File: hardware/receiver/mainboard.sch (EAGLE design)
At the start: 19 parts, among them J2 POWER_JACKPTH, J3 AVR_SPI_PRG_6PTH, Q1 MOSFET-NCHANNELAO3404A, U1 ATMEGA328P_TQFP, U2 RFM69HCW, U4 RELAY-9007

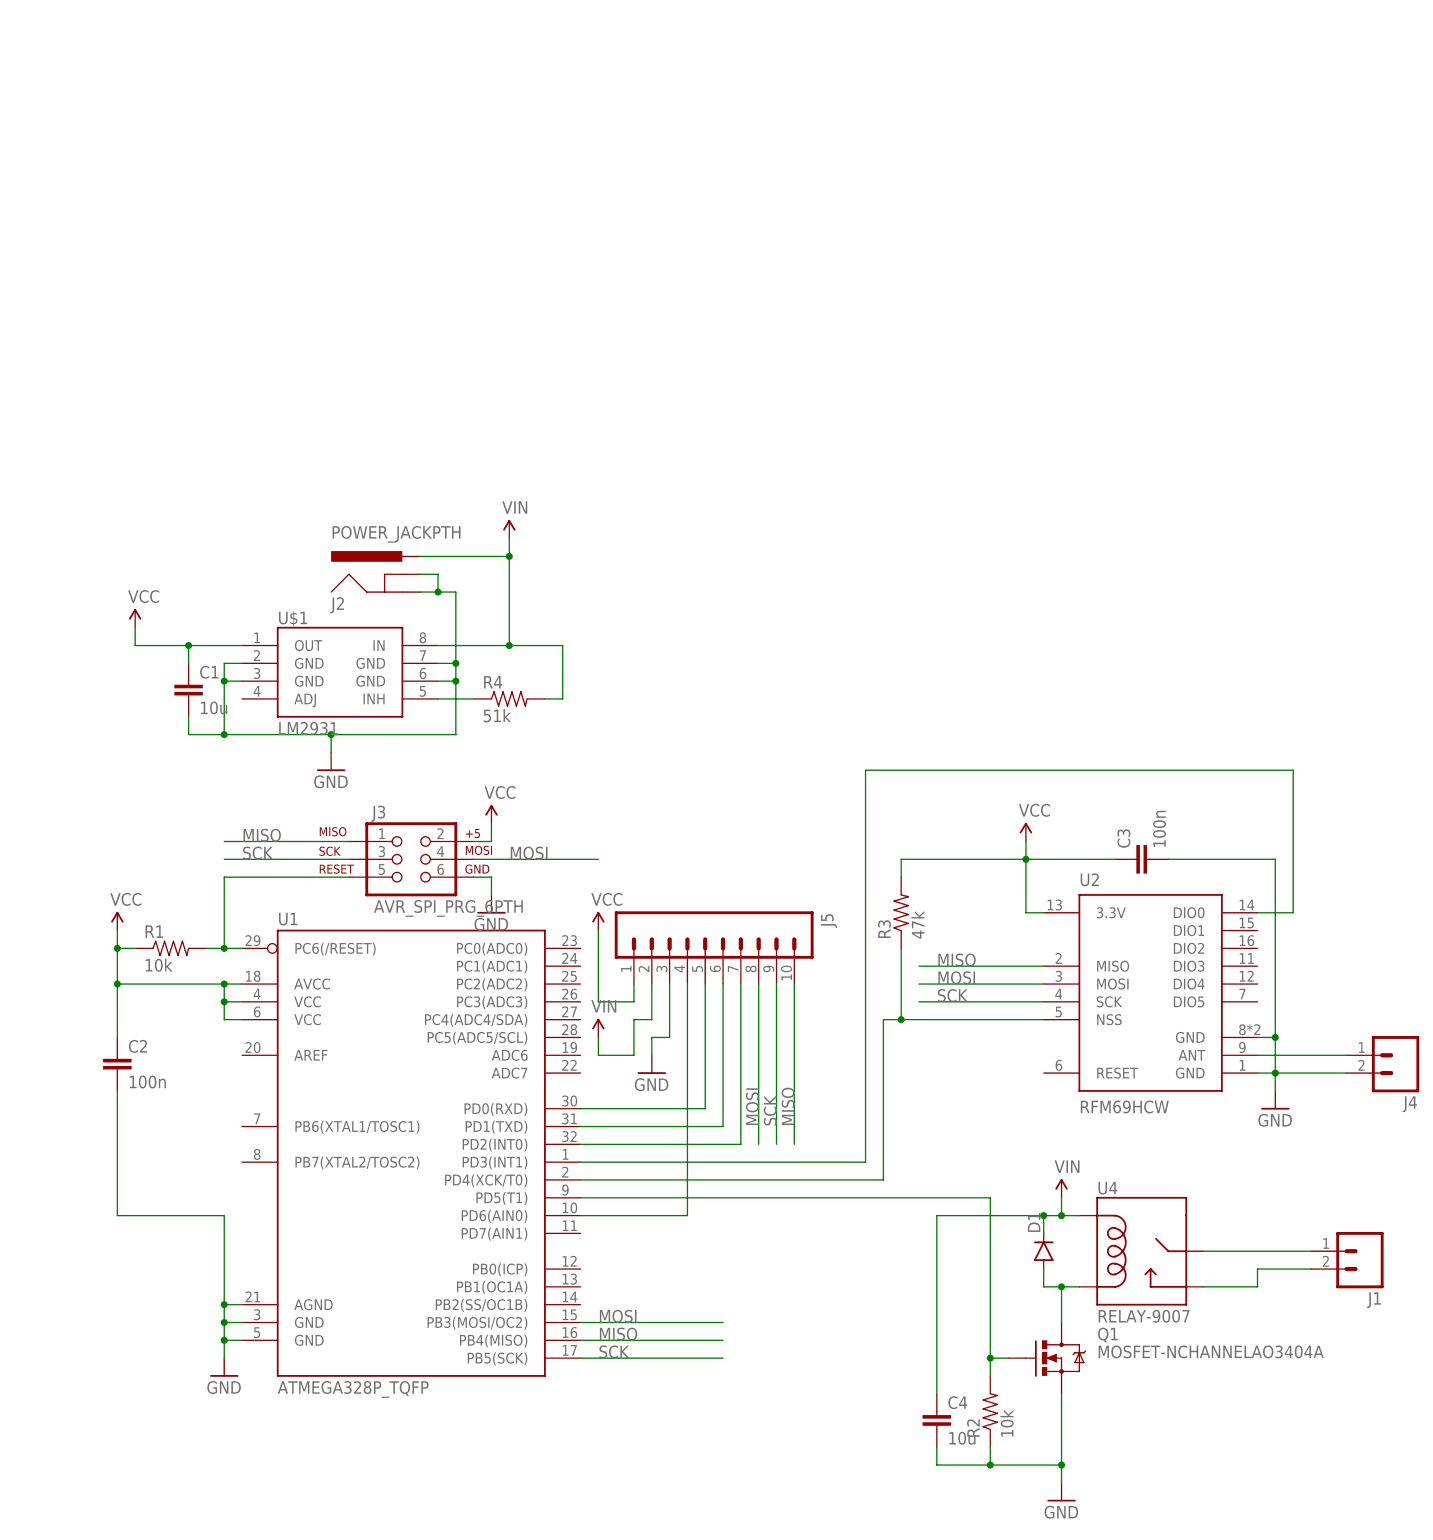
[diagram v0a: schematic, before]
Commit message: Added frames
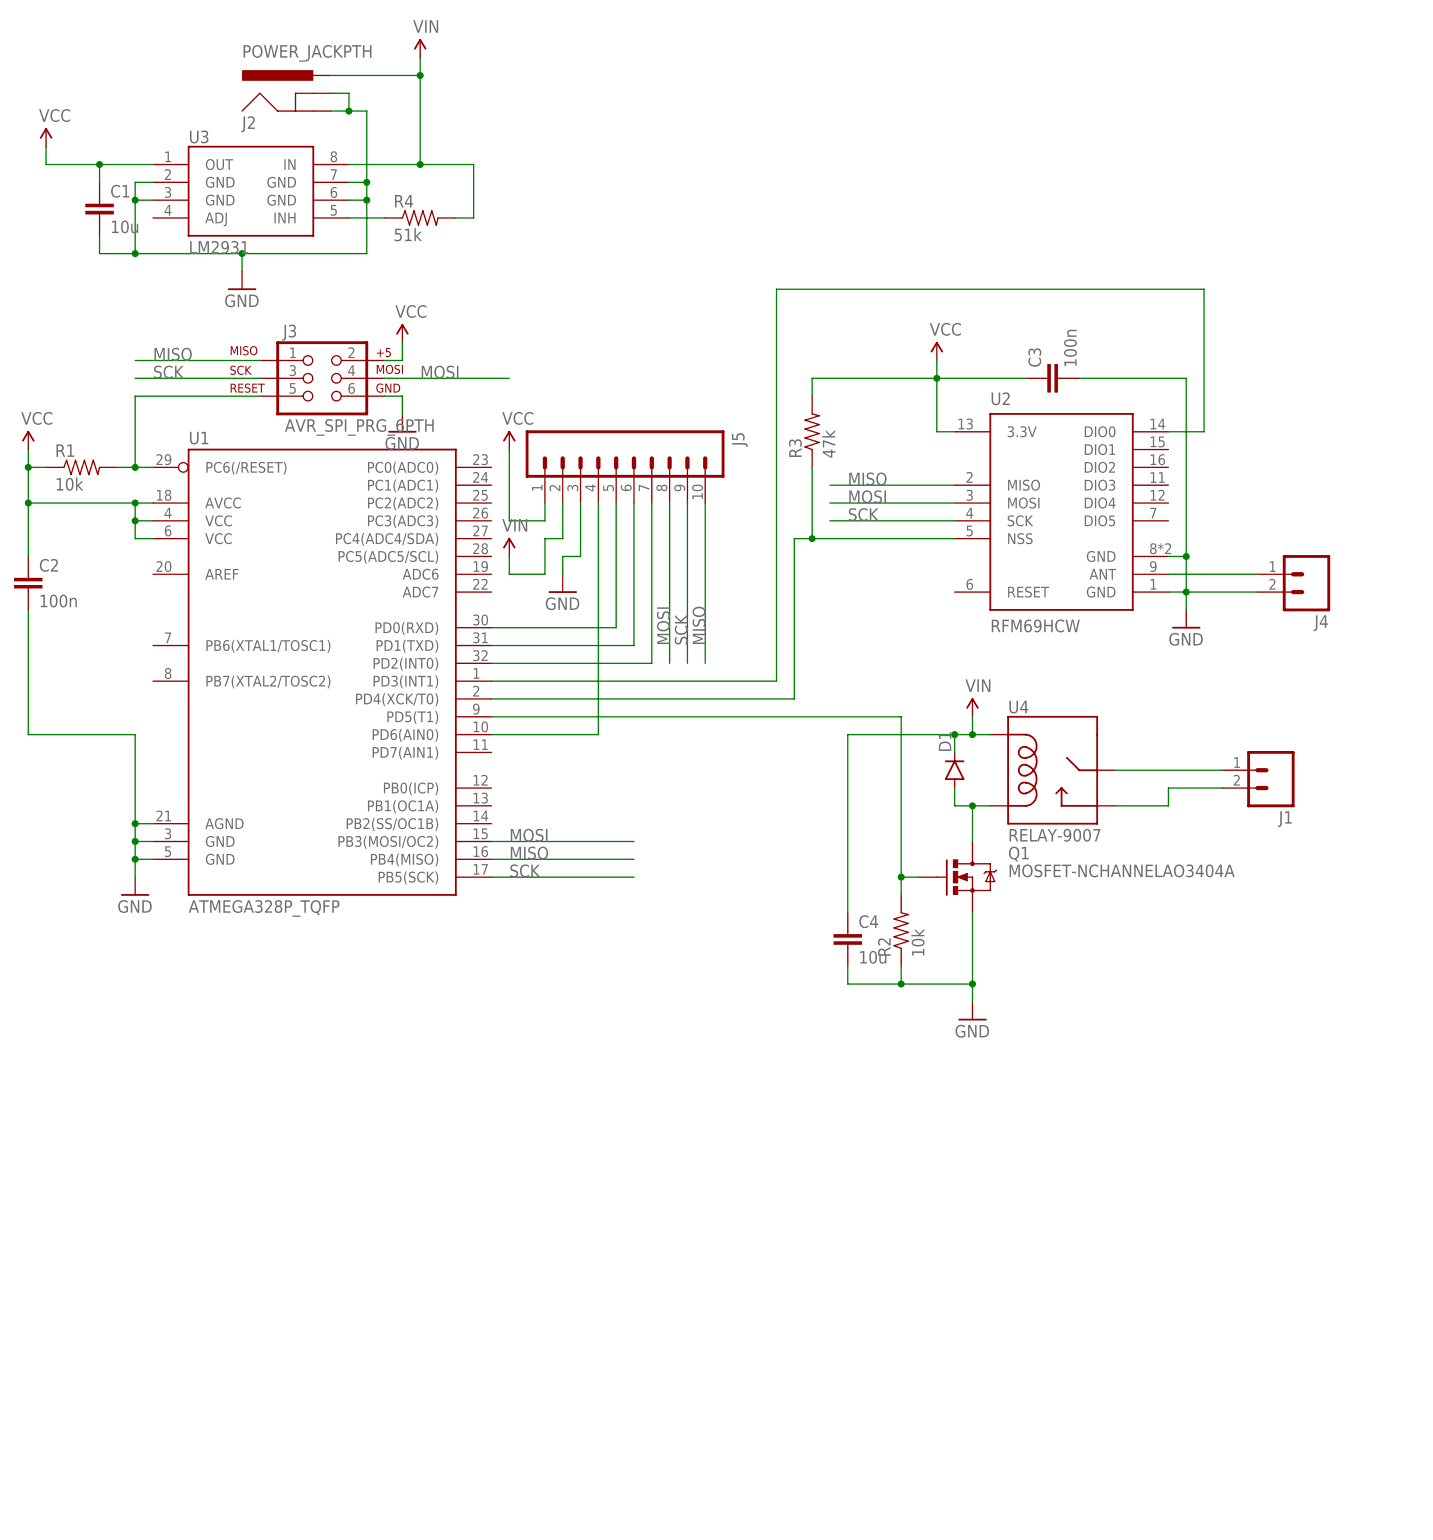
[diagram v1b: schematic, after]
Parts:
- removed U$1: LM2931, SparkFun-PowerIC:LM2931
- added U3: LM2931, SparkFun-PowerIC:LM2931
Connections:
- net GND: now also U3.GND@2, U3.GND@3, U3.GND@6, U3.GND@7; no longer U$1.GND@2, U$1.GND@3, U$1.GND@6, U$1.GND@7
- net N$19: now also U3.INH; no longer U$1.INH
- net VCC: now also U3.OUT; no longer U$1.OUT
- net VIN: now also U3.IN; no longer U$1.IN
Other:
- moved on the sheet: C1, C2, C3, C4, D1, J1, J2, J3, J4, J5, Q1, R1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
